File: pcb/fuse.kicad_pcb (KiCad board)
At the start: 2 copper layers, 137.2 x 85 mm, 65 parts, among them SW0 SW_PUSH, SW1 SW_PUSH, SW10 SW_PUSH, SW11 SW_PUSH, SW12 SW_PUSH, SW13 SW_PUSH, SW14 SW_PUSH, SW15 SW_PUSH, SW2 SW_PUSH, SW20 SW_PUSH, SW21 SW_PUSH, SW22 SW_PUSH, SW23 SW_PUSH, SW24 SW_PUSH, SW25 SW_PUSH, SW3 SW_PUSH, SW30 SW_PUSH, SW31 SW_PUSH, SW32 SW_PUSH, SW33 SW_PUSH, SW34 SW_PUSH, SW35 SW_PUSH, SW4 SW_PUSH, SW40 SW_PUSH, SW41 SW_PUSH, SW42 SW_PUSH, SW43 SW_PUSH, SW44 SW_PUSH, SW45 SW_PUSH, SW5 SW_PUSH, U1 ProMicro, U2 BatteryHole, U3 BatteryHole

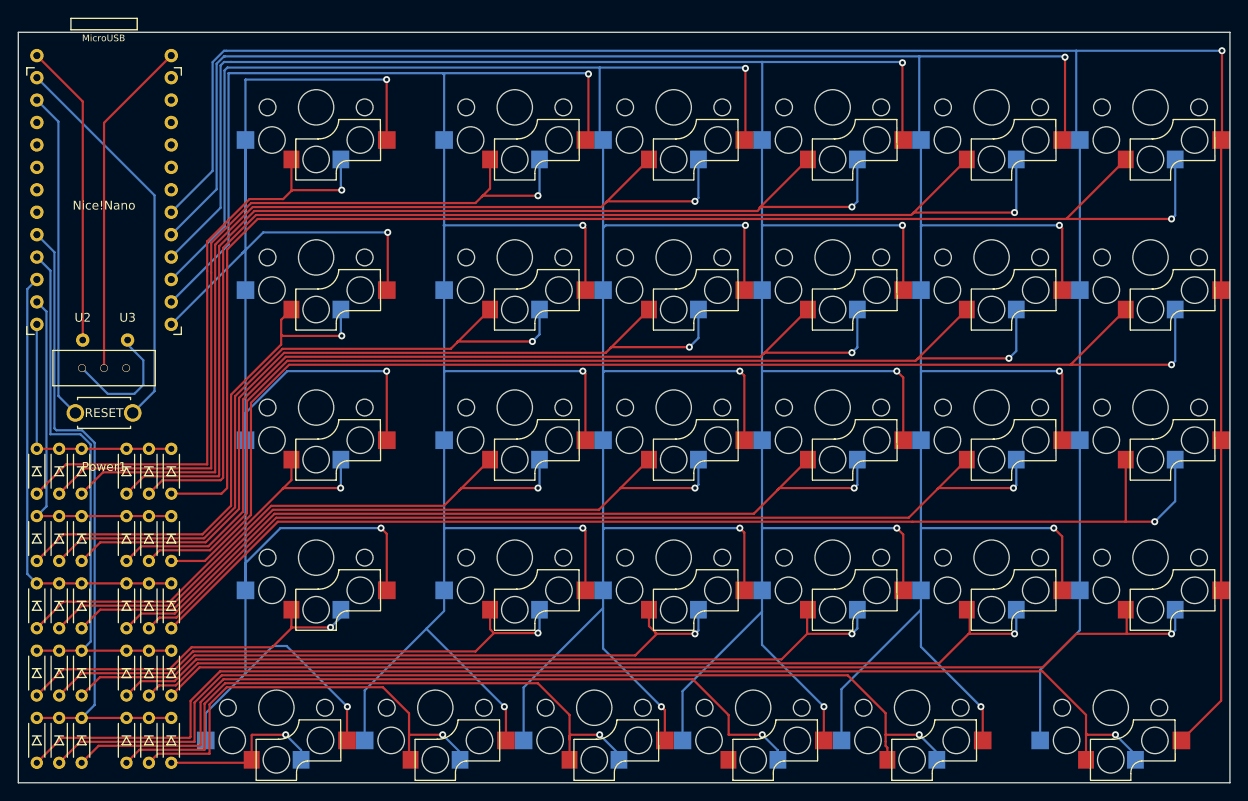
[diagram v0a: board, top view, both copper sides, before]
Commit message: Remove hotswap to cut down PCB size.
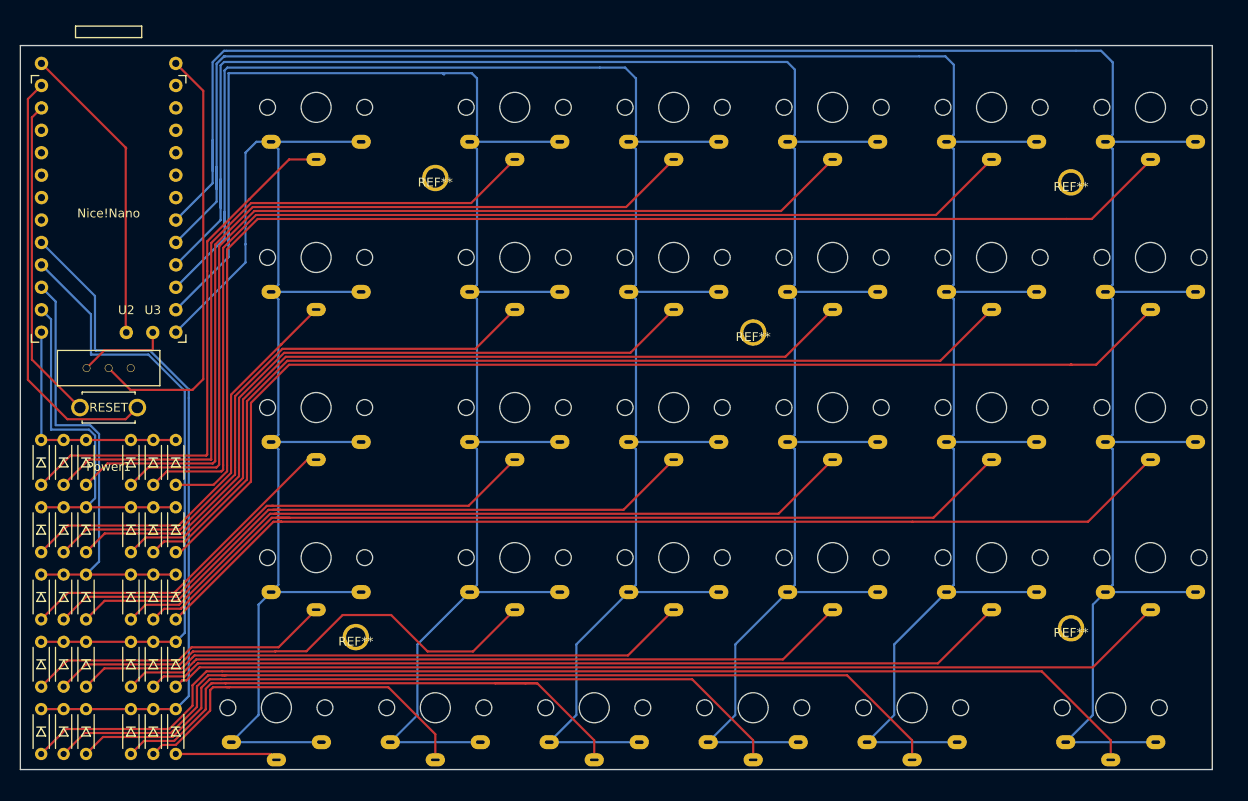
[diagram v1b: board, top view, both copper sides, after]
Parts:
- added REF**: M2Hole, fuse-kbd:M2Hole, F.Cu at (112.0, 53.5)
- added REF**: M2Hole, fuse-kbd:M2Hole, F.Cu at (76.0, 36.0)
- added REF**: M2Hole, fuse-kbd:M2Hole, F.Cu at (67.0, 88.0)
- added REF**: M2Hole, fuse-kbd:M2Hole, F.Cu at (148.0, 87.0)
- added REF**: M2Hole, fuse-kbd:M2Hole, F.Cu at (148.0, 36.5)
- SW0, SW10, SW20, SW30, SW45: footprint fuse-kbd:Choc_Hotswap_Reverse_15 -> fuse-kbd:Choc_Reverse_15
- SW1, SW11, SW12, SW13, SW14, SW15, SW2, SW21, SW22, SW23, SW24, SW25, SW3, SW31, SW32, SW33, SW34, SW35, SW4, SW40, SW41, SW42, SW43, SW44, SW5: footprint fuse-kbd:Choc_Hotswap_Reverse_1 -> fuse-kbd:Choc_Reverse
- moved U2 5.01 mm to (41.0, 53.5)
- moved U3 2.98 mm to (44.0, 53.5)
- moved D0 1.12 mm to (31.4, 65.7)
- moved D1 1.12 mm to (33.9, 65.7)
- moved D10 1.12 mm to (31.4, 73.3)
- moved D11 1.12 mm to (33.9, 73.3)
- moved D12 1.12 mm to (36.4, 73.3)
- moved D13 1.12 mm to (41.5, 73.3)
- moved D14 1.12 mm to (44.1, 73.3)
- moved D15 1.12 mm to (46.6, 73.3)
- moved D2 1.12 mm to (36.4, 65.7)
- moved D20 1.12 mm to (31.4, 80.9)
- moved D21 1.12 mm to (33.9, 80.9)
- moved D22 1.12 mm to (36.4, 80.9)
- moved D23 1.12 mm to (41.5, 80.9)
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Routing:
- net Col0: track 222.1 -> 150.0 mm, vias 5 -> 0
- net Col2: track 261.5 -> 208.0 mm, vias 5 -> 0
- net Col4: track 295.9 -> 242.8 mm, vias 5 -> 0
- net Col1: track 242.6 -> 191.7 mm, vias 5 -> 0
- net Col3: track 277.6 -> 226.7 mm, vias 5 -> 0
- net Col5: track 294.0 -> 258.4 mm, vias 1 -> 0
- net Net-(D5-Pad2): track 158.4 -> 140.4 mm, vias 1 -> 0
- net Net-(D15-Pad2): track 145.4 -> 127.8 mm, vias 1 -> 0
- net Net-(D14-Pad2): track 128.3 -> 111.5 mm, vias 1 -> 0
- net Net-(D4-Pad2): track 141.3 -> 124.9 mm, vias 1 -> 0
- net Net-(D13-Pad2): track 111.7 -> 96.1 mm, vias 1 -> 0
- net Net-(D3-Pad2): track 124.5 -> 109.2 mm, vias 1 -> 0
- net Net-(D12-Pad2): track 97.2 -> 83.1 mm, vias 1 -> 0
- net Net-(D2-Pad2): track 110.2 -> 96.2 mm, vias 1 -> 0
- net Net-(D25-Pad2): track 132.0 -> 118.3 mm, vias 1 -> 0
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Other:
- board size 137.2 x 85 mm -> 135 x 82 mm

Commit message: fix reset pin and footprints
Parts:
- removed the REF** at (112.0, 53.5)
- removed the REF** at (76.0, 36.0)
- removed U2: BatteryHole, fuse-kbd:BatteryPins
- added REF**: M2Hole, fuse-kbd:M2Hole, F.Cu at (76.0, 36.5)
- added U4: BatteryHole, fuse-kbd:BatteryPins, F.Cu at (42.5, 53.5)
- moved U3 5.00 mm to (39.0, 53.5)
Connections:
- Power1 pad 1: Net-(Power1-Pad1) -> B-
- Power1 pad 2: B+ -> Net-(Power1-Pad2)
- U1 pad 22: Net-(U1-Pad22) -> RESET
- U1 pad 24: RESET -> Net-(U1-Pad24)
- U3 pad 1: Net-(Power1-Pad1) -> Net-(Power1-Pad2)
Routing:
- net B+: track 49.3 -> 32.2 mm
- net Net-(Power1-Pad1): track 10.3 -> 0.00 mm
- net RESET: track 48.8 -> 43.3 mm
- net Net-(Power1-Pad2): track 0.00 -> 4.03 mm
- net B-: track 34.6 -> 36.6 mm
- net GND: track 36.6 -> 35.7 mm
